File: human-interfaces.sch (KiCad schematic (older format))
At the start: 31 parts

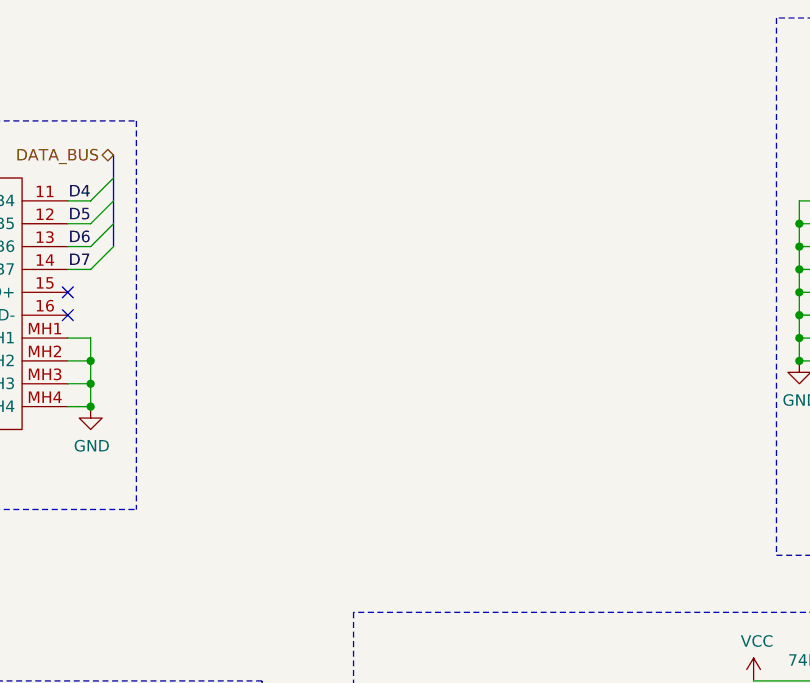
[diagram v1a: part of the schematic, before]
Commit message: General edits; removed floating inputs
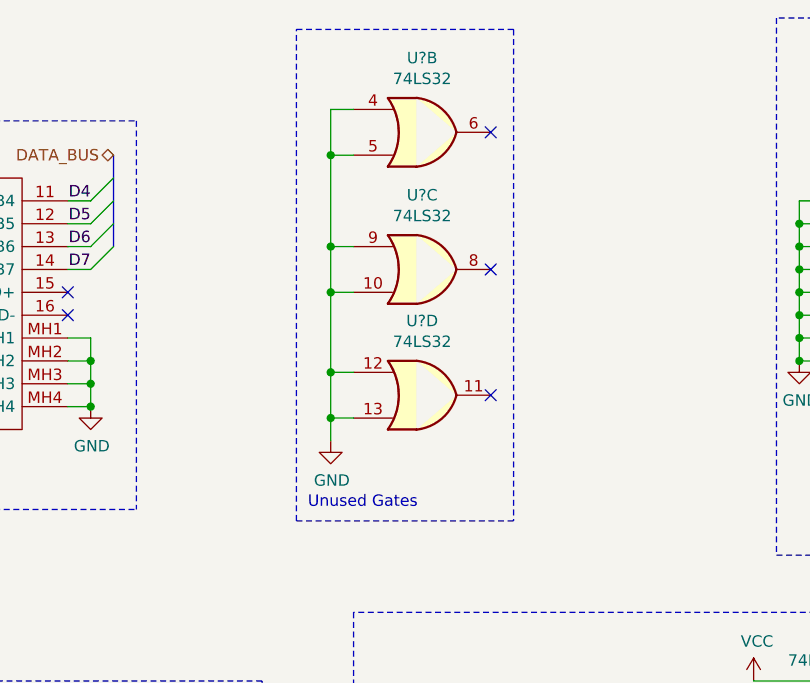
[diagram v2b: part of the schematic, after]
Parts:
- added U? (x3): 74LS32, symbol 74xx:74LS32
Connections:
- net GND: now also U?.10, U?.12, U?.13, U?.4, U?.5, U?.9
- no-connect marks 2 -> 5
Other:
- note added: "Unused Gates"

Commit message: Updates to pass ERC
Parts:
- added R? (x2): R, symbol Device:R
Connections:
- net GND: now also R?.2
- net VCC: now also R?.1
- net V0: now reaches DS?.3 (V0)
- net V0: now also R?.1, R?.2
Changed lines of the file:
@@
 $EndDescr
 Text HLabel 1100 5650 0    50   BiDi ~ 0
-DATA_BUS
+D[0..15]
 Text HLabel 2700 1350 0    50   Input ~ 0
-ADDRESS_BUS
+A[0..19]
 Text HLabel 850  7350 3    50   Input ~ 0
 ~LED_CS
@@
 ~WR
 Text HLabel 6600 3650 0    50   BiDi ~ 0
-DATA_BUS
+D[0..15]
 Entry Wire Line
 	6700 3850 6600 3750
@@
 ~WR
 Text HLabel 8950 4350 0    50   BiDi ~ 0
-DATA_BUS
+D[0..15]
 Entry Wire Line
 	9050 4550 8950 4450
@@
 $EndComp
 Text HLabel 2700 2550 2    50   BiDi ~ 0
-DATA_BUS
+D[0..15]
 Text HLabel 4200 1250 0    50   BiDi ~ 0
-DATA_BUS
+D[0..15]
 Wire Wire Line
 	4000 2050 4100 2050
@@
 Text Notes 4800 3650 2    50   ~ 0
 Power Decoupling
-Wire Notes Line
-	1200 1100 4300 1100
-Text Notes 1250 2750 0    50   ~ 0
+Text Notes 850  2750 0    50   ~ 0
 4x20 LCD Display\n0xFFD0, 0xFFD2, 0xFFD4, 0xFFD6
 Wire Notes Line
-	1200 2800 4300 2800
-Wire Notes Line
-	1200 1100 1200 2800
+	800  1100 800  2800
 Wire Notes Line
 	4300 1100 4300 2800
@@
 Wire Notes Line
 	11050 3250 5250 3250
-Wire Bus Line
-	2700 1350 2700 1750
-Wire Bus Line
-	4200 1250 4200 1650
-Wire Bus Line
-	2700 2150 2700 2550
-Wire Bus Line
-	8950 4350 8950 5150
-Wire Bus Line
-	6600 3650 6600 4450
-Wire Bus Line
-	1100 5650 1100 6450
-Wire Bus Line
-	10500 1250 10500 2050
 Text Notes 10950 2950 2    50   ~ 0
 DIP Switches\n0xFFCA
@@
 	10400 1450 10500 1350
 Text HLabel 10500 1250 2    50   BiDi ~ 0
-DATA_BUS
+D[0..15]
 $Comp
 L 74xx:74LS244 U?
@@
 Text HLabel 8600 2350 0    50   Input ~ 0
 ~DIP_CS
+$Comp
+L power:VCC #PWR?
+U 1 1 6258205E
+P 1000 1450
+F 0 "#PWR?" H 1000 1300 50  0001 C CNN
+F 1 "VCC" H 1015 1623 50  0000 C CNN
+F 2 "" H 1000 1450 50  0001 C CNN
+F 3 "" H 1000 1450 50  0001 C CNN
+	1    1000 1450
+	1    0    0    -1
+$EndComp
+$Comp
+L power:GND #PWR?
+U 1 1 625829F1
+P 1000 2150
+F 0 "#PWR?" H 1000 1900 50  0001 C CNN
+F 1 "GND" H 1005 1977 50  0000 C CNN
+F 2 "" H 1000 2150 50  0001 C CNN
+F 3 "" H 1000 2150 50  0001 C CNN
+	1    1000 2150
+	1    0    0    -1
+$EndComp
+$Comp
+L Device:R R?
+U 1 1 62583966
+P 1000 1600
+F 0 "R?" H 1070 1646 50  0000 L CNN
+F 1 "R" H 1070 1555 50  0000 L CNN
+F 2 "" V 930 1600 50  0001 C CNN
+F 3 "~" H 1000 1600 50  0001 C CNN
+	1    1000 1600
+	1    0    0    -1
+$EndComp
+$Comp
+L Device:R R?
+U 1 1 62585A0D
+P 1000 2000
+F 0 "R?" H 1070 2046 50  0000 L CNN
+F 1 "R" H 1070 1955 50  0000 L CNN
+F 2 "" V 930 2000 50  0001 C CNN
+F 3 "~" H 1000 2000 50  0001 C CNN
+	1    1000 2000
+	1    0    0    -1
+$EndComp
+Wire Wire Line
+	1000 1750 1000 1850
+Text Label 1000 1800 2    50   ~ 0
+V0
+Text Label 2900 1650 2    50   ~ 0
+V0
+Wire Notes Line
+	800  2800 4300 2800
+Wire Notes Line
+	800  1100 4300 1100
+Wire Bus Line
+	2700 1350 2700 1750
+Wire Bus Line
+	4200 1250 4200 1650
+Wire Bus Line
+	2700 2150 2700 2550
+Wire Bus Line
+	8950 4350 8950 5150
+Wire Bus Line
+	6600 3650 6600 4450
+Wire Bus Line
+	1100 5650 1100 6450
+Wire Bus Line
+	10500 1250 10500 2050
 $EndSCHEMATC

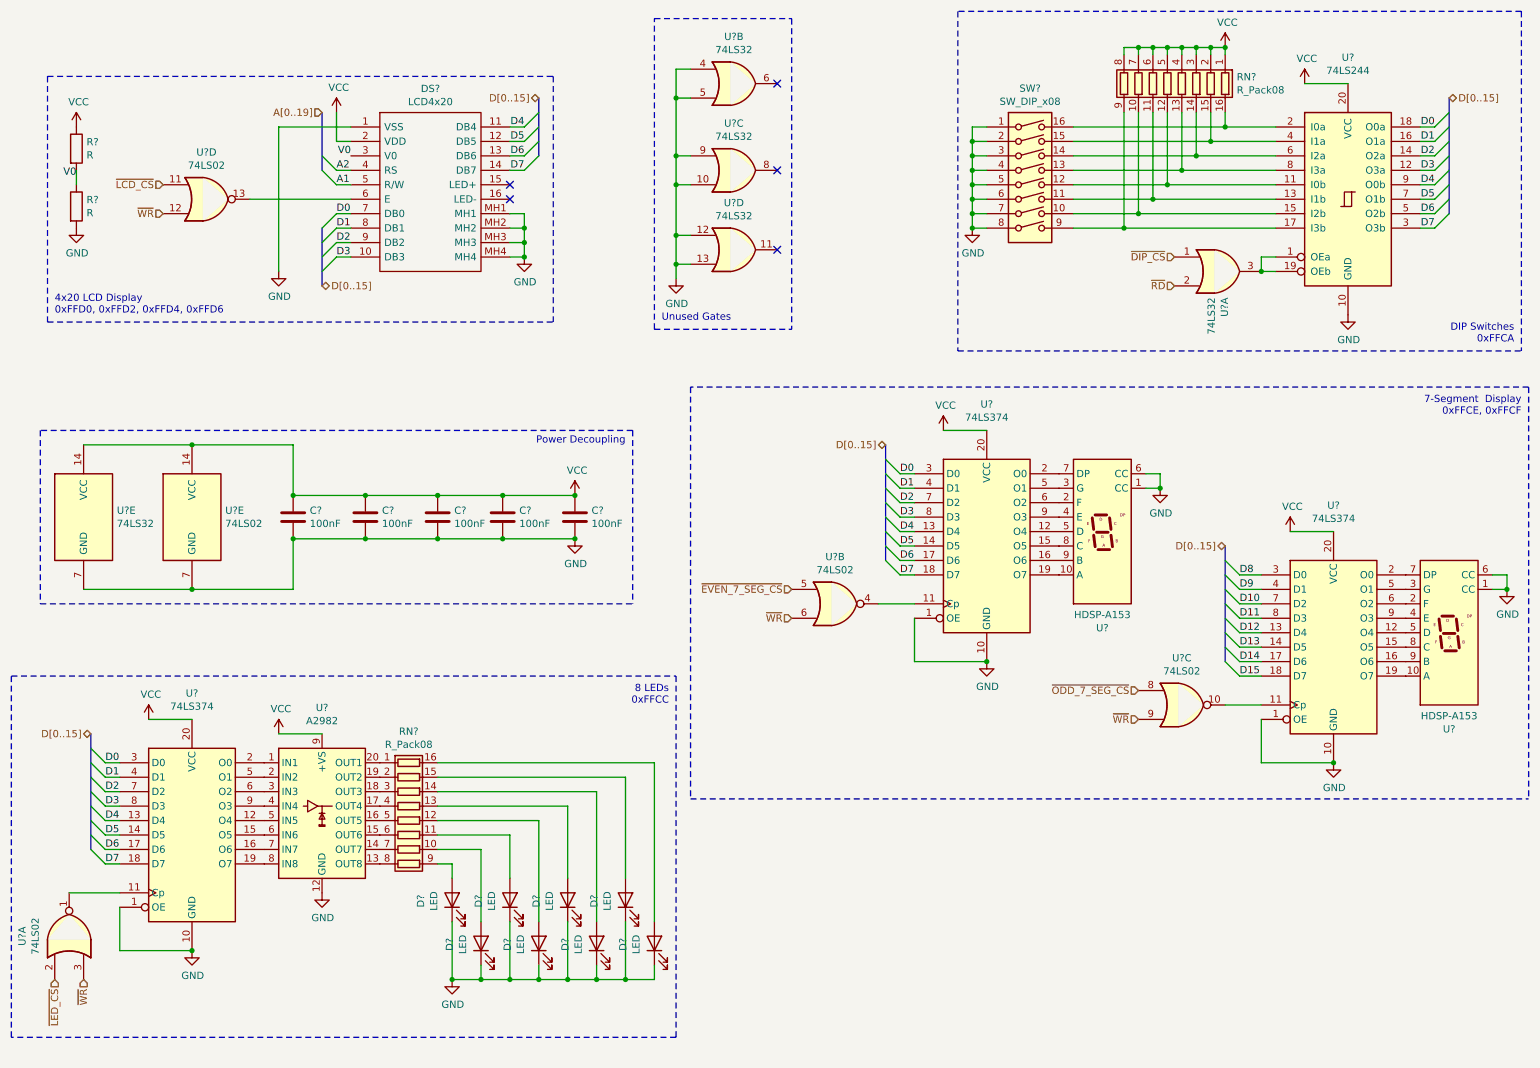
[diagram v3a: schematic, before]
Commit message: Assign footprints for most symbols
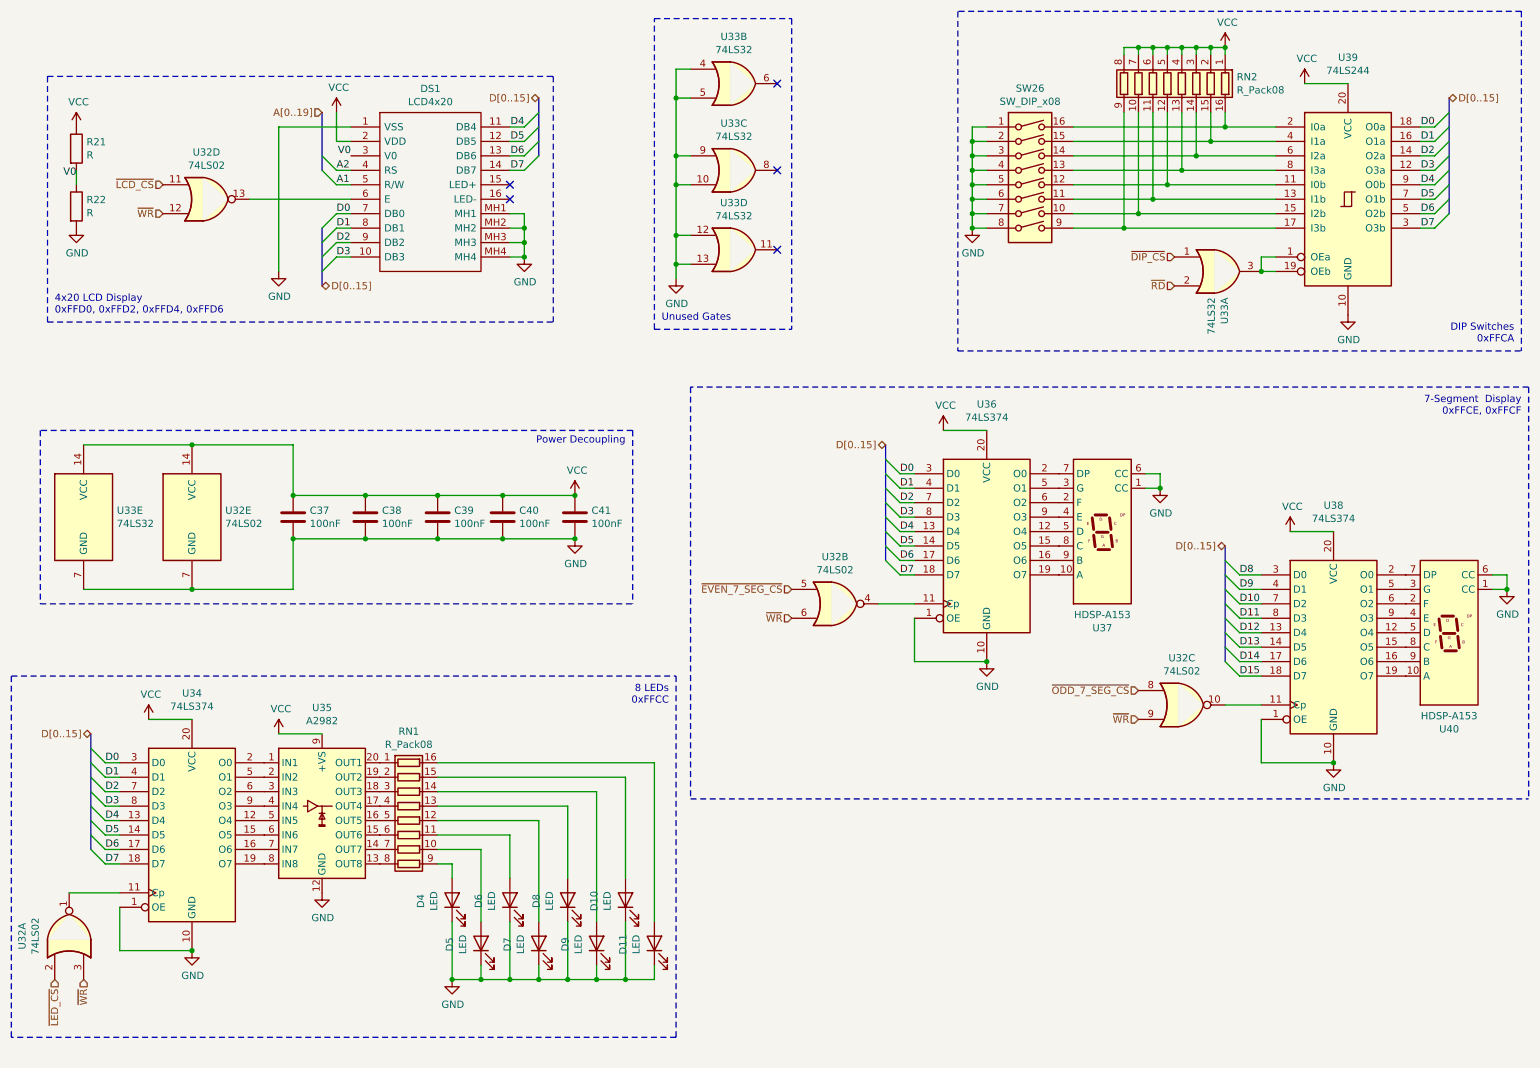
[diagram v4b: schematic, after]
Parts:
- C37, C38, C39, C40, C41: renamed from C?; footprint (none) -> Capacitor_THT:C_Rect_L4.0mm_W2.5mm_P2.50mm
- D10, D11, D4, D5, D6, D7, D8, D9: renamed from D?; footprint (none) -> LED_THT:LED_D5.0mm
- DS1: renamed from DS?; footprint LCD4x20 -> Libraries:LCD4x20
- R21, R22: renamed from R?; footprint (none) -> Resistor_THT:R_Axial_DIN0207_L6.3mm_D2.5mm_P10.16mm_Horizontal
- RN1, RN2: renamed from RN?; footprint (none) -> Package_DIP:DIP-16_W7.62mm
- SW26: renamed from SW?; footprint (none) -> Package_DIP:DIP-16_W7.62mm
- U32, U33, U34, U36, U38, U39: renamed from U?; footprint (none) -> Package_DIP:DIP-20_W7.62mm
- gave numbers to parts that had none: 3

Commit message: assign footprints and edits
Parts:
- removed U35: A2982, Package_SO:SOIC-20W_7.5x12.8mm_P1.27mm, symbol Transistor_Array:A2982
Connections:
- net GND: no longer D10.1 (K), D11.1 (K), D4.1 (K), D5.1 (K), D6.1 (K), D7.1 (K), D8.1 (K), D9.1 (K)
- net VCC: now also D10.2 (A), D11.2 (A), D4.2 (A), D5.2 (A), D6.2 (A), D7.2 (A), D8.2 (A), D9.2 (A)
- net at U34.12 (O4): now also RN1.5 (R5.1)
- net at U34.15 (O5): now also RN1.6 (R6.1)
- net at U34.16 (O6): now also RN1.7 (R7.1)
- net at U34.19 (O7): now also RN1.8 (R8.1)
- net at U34.2 (O0): now also RN1.1 (R1.1)
- net at U34.5 (O1): now also RN1.2 (R2.1)
- net at U34.6 (O2): now also RN1.3 (R3.1)
- net at U34.9 (O3): now also RN1.4 (R4.1)
- net at RN1.10 (R7.2): now also D10.1 (K); no longer D5.2 (A)
- net at RN1.9 (R8.2): now also D11.1 (K); no longer D4.2 (A)
- net at RN1.11 (R6.2): now also D9.1 (K); no longer D6.2 (A)
- net at RN1.12 (R5.2): now also D8.1 (K); no longer D7.2 (A)
- net at RN1.13 (R4.2): now also D7.1 (K); no longer D8.2 (A)
- net at RN1.14 (R3.2): now also D6.1 (K); no longer D9.2 (A)
- net at RN1.15 (R2.2): now also D5.1 (K); no longer D10.2 (A)
- net at RN1.16 (R1.2): now also D4.1 (K); no longer D11.2 (A)
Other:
- moved on the sheet: D10, D11, D4, D5, D6, D7, D8, D9, DS1, R21, R22, RN1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

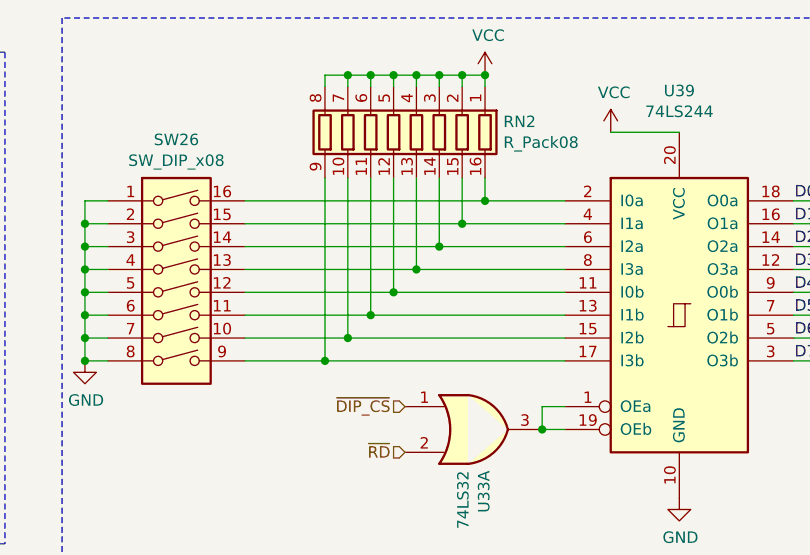
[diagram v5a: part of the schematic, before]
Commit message: Route data bus lines, most chip selects
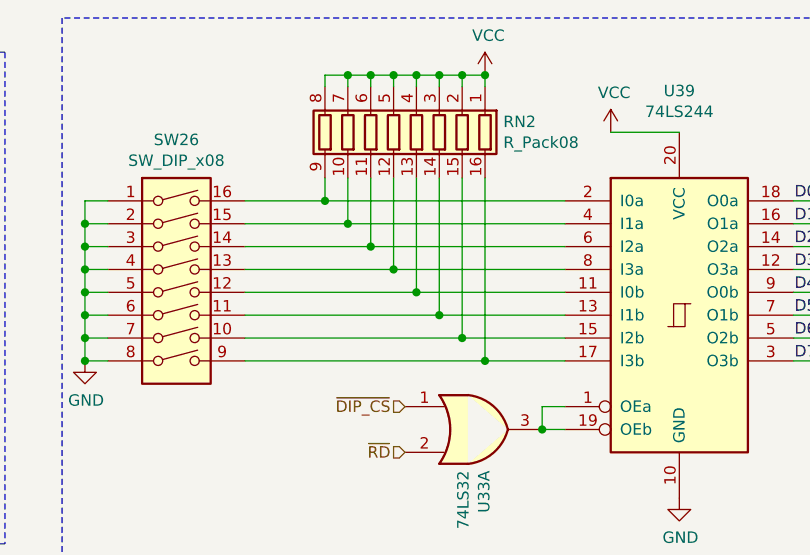
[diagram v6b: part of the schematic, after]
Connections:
- net at SW26.10, U39.15 (I2b): now also RN2.15 (R2.2); no longer RN2.10 (R7.2)
- net at SW26.11, U39.13 (I1b): now also RN2.14 (R3.2); no longer RN2.11 (R6.2)
- net at SW26.12, U39.11 (I0b): now also RN2.13 (R4.2); no longer RN2.12 (R5.2)
- net at SW26.13, U39.8 (I3a): now also RN2.12 (R5.2); no longer RN2.13 (R4.2)
- net at SW26.14, U39.6 (I2a): now also RN2.11 (R6.2); no longer RN2.14 (R3.2)
- net at SW26.15, U39.4 (I1a): now also RN2.10 (R7.2); no longer RN2.15 (R2.2)
- net at SW26.16, U39.2 (I0a): now also RN2.9 (R8.2); no longer RN2.16 (R1.2)
- net at SW26.9, U39.17 (I3b): now also RN2.16 (R1.2); no longer RN2.9 (R8.2)
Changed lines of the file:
@@
 Wire Wire Line
 	8250 950  8250 900
-Wire Wire Line
-	8250 2150 7900 2150
-Connection ~ 8250 2150
-Wire Wire Line
-	8250 1350 8250 2150
-Wire Wire Line
-	8350 2050 9300 2050
-Connection ~ 8350 2050
-Wire Wire Line
-	8350 1350 8350 2050
-Wire Wire Line
-	8450 1950 7900 1950
-Connection ~ 8450 1950
-Wire Wire Line
-	8450 1350 8450 1950
-Wire Wire Line
-	8550 1850 9300 1850
-Connection ~ 8550 1850
-Wire Wire Line
-	8550 1350 8550 1850
-Wire Wire Line
-	8650 1750 7900 1750
-Connection ~ 8650 1750
-Wire Wire Line
-	8650 1350 8650 1750
-Wire Wire Line
-	8750 1650 9300 1650
-Connection ~ 8750 1650
-Wire Wire Line
-	8750 1350 8750 1650
-Wire Wire Line
-	8850 1550 7900 1550
-Connection ~ 8850 1550
-Wire Wire Line
-	8850 1350 8850 1550
-Wire Wire Line
-	8950 1450 9300 1450
-Connection ~ 8950 1450
-Wire Wire Line
-	8950 1350 8950 1450
-Wire Wire Line
-	9300 2150 8250 2150
-Wire Wire Line
-	7900 2050 8350 2050
-Wire Wire Line
-	9300 1950 8450 1950
-Wire Wire Line
-	7900 1850 8550 1850
-Wire Wire Line
-	9300 1750 8650 1750
-Wire Wire Line
-	7900 1650 8750 1650
-Wire Wire Line
-	9300 1550 8850 1550
-Wire Wire Line
-	7900 1450 8950 1450
 $Comp
 L Device:R_Pack08 RN2
@@
 Text HLabel 5950 4650 0    50   Input ~ 0
 ~EVEN_7_SEG_CS
+Wire Wire Line
+	7900 2050 8850 2050
+Wire Wire Line
+	7900 1950 8750 1950
+Wire Wire Line
+	7900 1850 8650 1850
+Wire Wire Line
+	7900 1750 8550 1750
+Wire Wire Line
+	7900 1650 8450 1650
+Wire Wire Line
+	7900 1550 8350 1550
+Wire Wire Line
+	7900 1450 8250 1450
+Wire Wire Line
+	8250 1350 8250 1450
+Connection ~ 8250 1450
+Wire Wire Line
+	8250 1450 9300 1450
+Wire Wire Line
+	8350 1350 8350 1550
+Connection ~ 8350 1550
+Wire Wire Line
+	8350 1550 9300 1550
+Wire Wire Line
+	8450 1350 8450 1650
+Connection ~ 8450 1650
+Wire Wire Line
+	8450 1650 9300 1650
+Wire Wire Line
+	8550 1350 8550 1750
+Connection ~ 8550 1750
+Wire Wire Line
+	8550 1750 9300 1750
+Wire Wire Line
+	8650 1350 8650 1850
+Connection ~ 8650 1850
+Wire Wire Line
+	8650 1850 9300 1850
+Wire Wire Line
+	8750 1350 8750 1950
+Connection ~ 8750 1950
+Wire Wire Line
+	8750 1950 9300 1950
+Wire Wire Line
+	7900 2150 8950 2150
+Wire Wire Line
+	8850 1350 8850 2050
+Connection ~ 8850 2050
+Wire Wire Line
+	8850 2050 9300 2050
+Wire Wire Line
+	8950 1350 8950 2150
 Wire Bus Line
 	2550 1200 2550 1600
@@
 	2550 2000 2550 2400
 Wire Bus Line
-	10500 1250 10500 2050
+	6600 3650 6600 4450
 Wire Bus Line
 	8950 4350 8950 5150
 Wire Bus Line
-	6600 3650 6600 4450
+	10500 1250 10500 2050
 Wire Bus Line
 	1500 6000 1500 6800
+Connection ~ 8950 2150
+Wire Wire Line
+	8950 2150 9300 2150
 $EndSCHEMATC
